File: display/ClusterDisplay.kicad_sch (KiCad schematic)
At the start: 110 parts, among them J1 Verdin iMX95 Hexa 8GB WB IT, J10 RTC coin cell, J11 Molex KK-254 22-27-2041, rota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, J2 Phoenix MKDS 1,5/3-5,08 power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, J3 Molex KK-254 22-27-2031 priva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, J4 TST040HDBC-42 panel, J8 Samtec TSW-108-07-G-S JTAG (b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, J9 Samtec TSW-104-07-G-S buttons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, Q1 PMV55ENEA (AEC-Q101, 60V/20V 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, Q2 PMV55ENEA (AEC-Q101, 60V/20V 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, Q3 PMV55ENEA ignition wake pulld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, U1 LM74930-Q1, U2 LM61460-Q1, U3 TLV767-Q1, U4 TCAN1044V-Q1, U6 TPS65131-Q1, U7 TPS61165-Q1

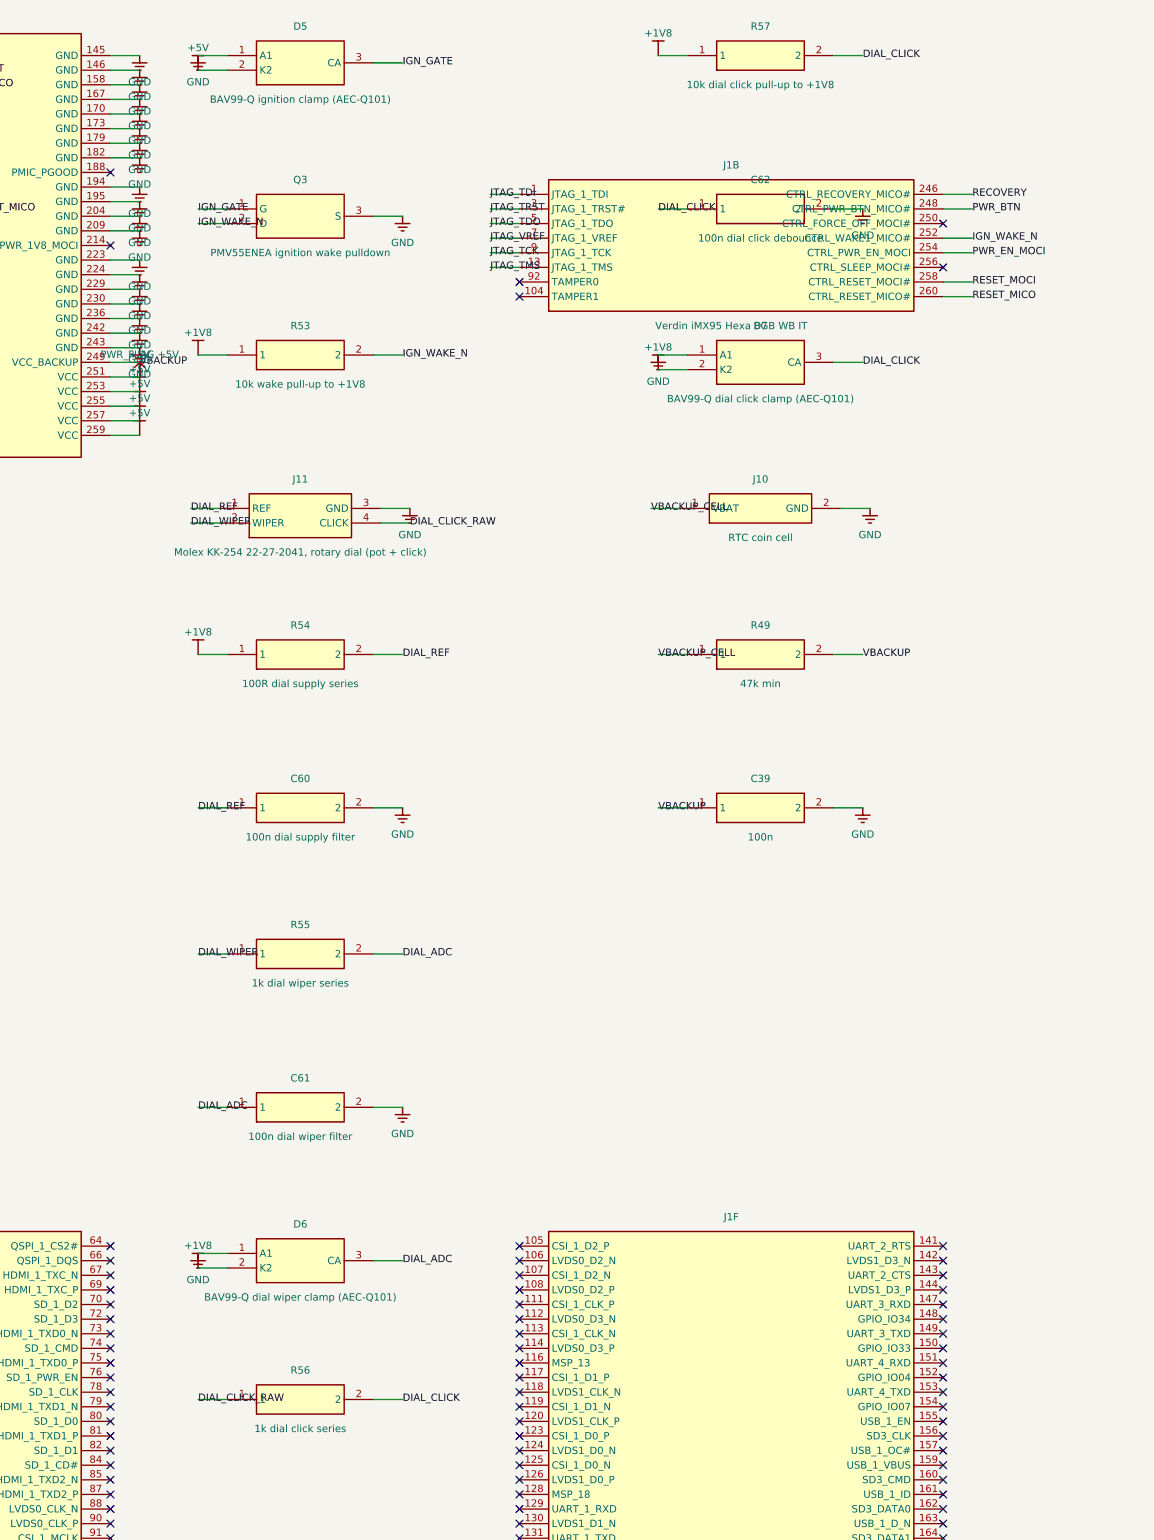
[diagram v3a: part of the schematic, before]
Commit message: display: dial interface for a Piher PSC-360 (switched 5V, scaled analog signal) plus separate click input
PSC-360 is a contactless Hall angle sensor with endless rotation; its switch output is an angle
threshold, not a push button, so J11 keeps a separate click input. Sensor 5V comes through a
TPS22918-Q1 load switch controlled by the Verdin's CTRL_SLEEP_MOCI# so it is off in suspend; the
0-5.5V ratiometric output is divided to fit the 2.1V ADC limit. ERC 0 violations, routed clean,
BOM lists the stocked PSC360G2-F1A-C0000-ERA360-05K for prototyping.

Co-Authored-By: Claude Sonnet 5.5 <noreply@anthropic.com>
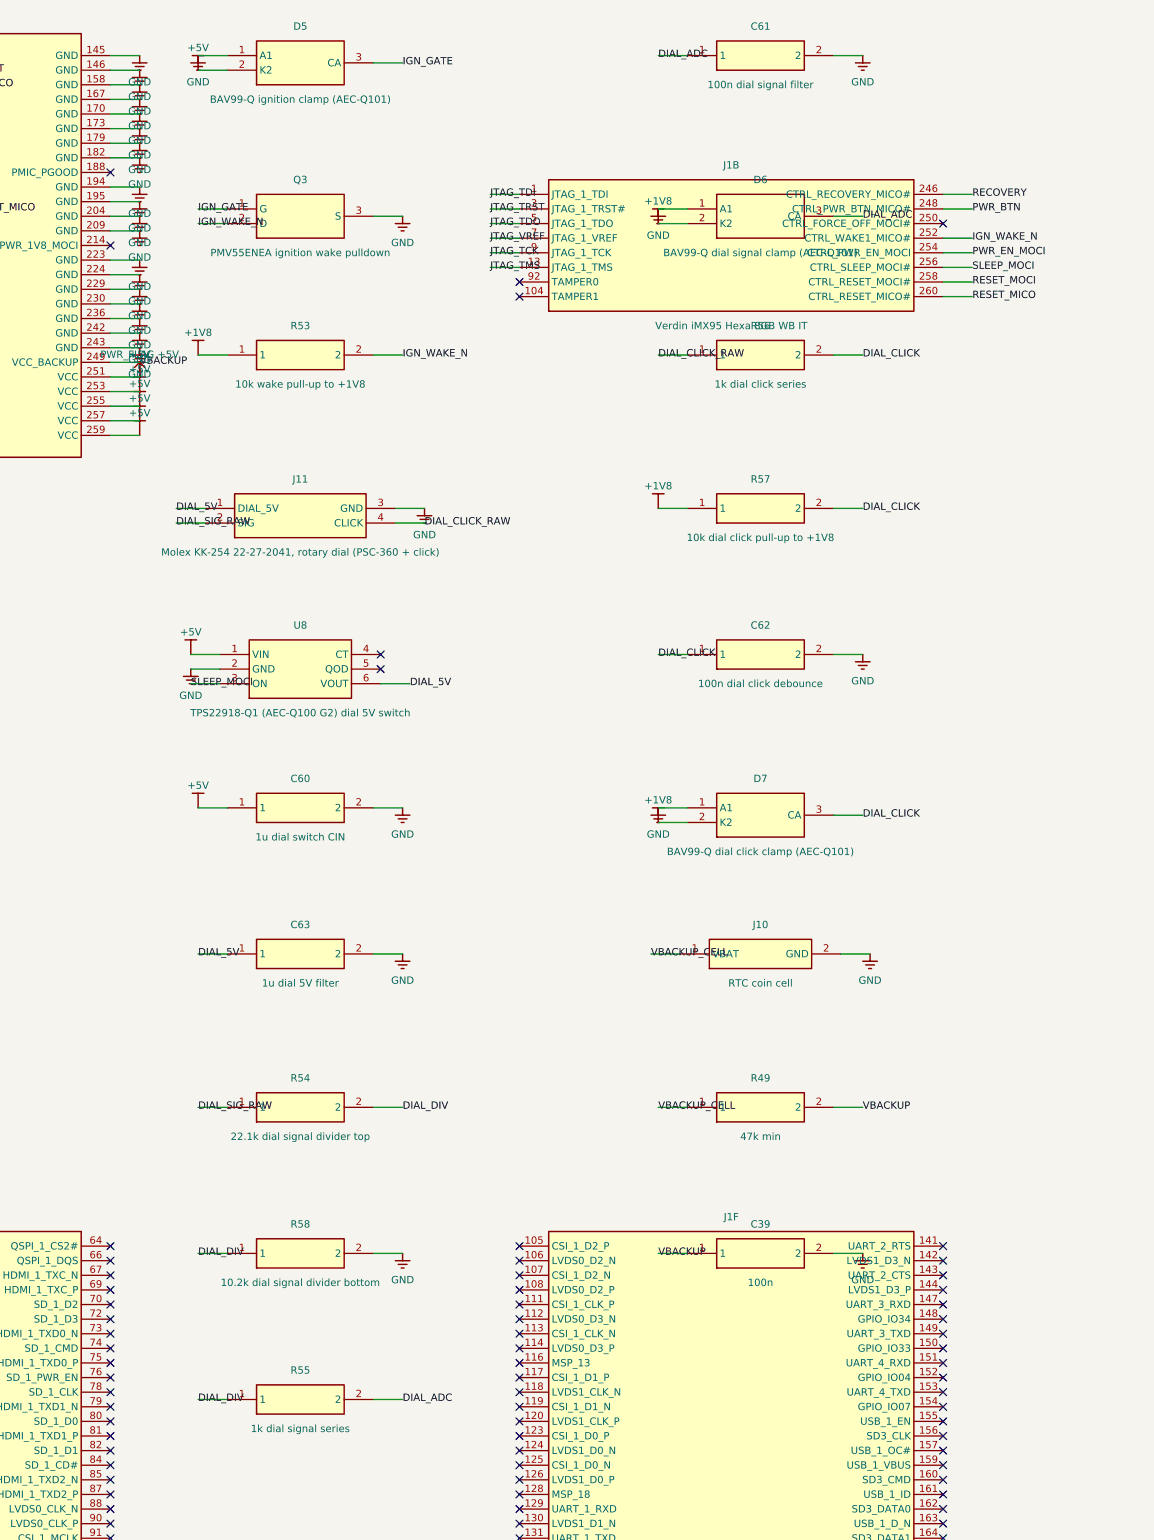
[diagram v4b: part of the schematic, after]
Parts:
- added C63: 1u dial 5V filter, Capacitor_SMD:C_0603_1608Metric, symbol ClusterDisplay:C
- added R58: 10.2k dial signal divider bottom, Resistor_SMD:R_0603_1608Metric, symbol ClusterDisplay:R
- added U8: TPS22918-Q1 (AEC-Q100 G2) dial 5V switch, Package_TO_SOT_SMD:SOT-23-6, symbol ClusterDisplay:TPS22918-Q1
- C60: value 100n dial supply filter -> 1u dial switch CIN
- C61: value 100n dial wiper filter -> 100n dial signal filter
- D6: value BAV99-Q dial wiper clamp (AEC-Q101) -> BAV99-Q dial signal clamp (AEC-Q101)
- J11: value Molex KK-254 22-27-2041, rotary dial (pot + click) -> Molex KK-254 22-27-2041, rotary dial (PSC-360 + click)
- R54: value 100R dial supply series -> 22.1k dial signal divider top
- R55: value 1k dial wiper series -> 1k dial signal series
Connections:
- net +1V8: no longer R54.1
- net +5V: now also C60.1, U8.1 (VIN)
- net GND: now also C63.2, R58.2, U8.2 (GND)
- net SLEEP_MOCI: now reaches J1.256 (CTRL_SLEEP_MOCI#)
- net SLEEP_MOCI: now also U8.3 (ON)
- removed net DIAL_REF: C60.1, J11.1 (REF), R54.2
- net DIAL_WIPER renamed DIAL_DIV
- net DIAL_DIV: now also R54.2, R58.1; no longer J11.2 (WIPER)
- new net DIAL_5V: C63.1, J11.1 (DIAL_5V), U8.6 (VOUT)
- new net DIAL_SIG_RAW: J11.2 (SIG), R54.1
- no-connect marks 197 -> 198

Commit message: Fix review findings: MOSFET pinout, gauges surge front end, converter cells, DSI
Review of 2026-10-03 found real defects; fixes and measured results:
- Nexperia PMV55ENEA/PMV37ENEA pinout is G=1, S=2, D=3: display Q1-Q3 and
  gauges Q2 had source/drain swapped. Fixed in both schematics.
- gauges/ now has the same LM74930-Q1 surge-protected front end as display/
  (5 mohm sense, OV clamp), a 5 A/32 V blade fuse on display/ (the MF-RG500 PTC
  was a 16 V part), and sender inputs with series resistor, clamp and filter.
- Converters are placed as cells around their ICs (tools/cellplace.py).
  display: SW_5V 55.6 -> 11.6 mm, boost/inverter/backlight SW 75 -> 7-13 mm,
  LM61460 input caps 57 -> 4.7-7.5 mm. gauges: SW 26.8 -> 8.7 mm, input caps 4.5 mm.
- display DSI pairs are planned by dsi_route.py after the autorouter: legs
  10.6-11.2 mm, at most 0.6 mm skew in a pair (was 64-85 mm, 21 mm skew).
- In1 is a GND plane for the router on display/ (about 925 mm of slow signals
  still cross it, down from 2615); forbidding signals there left 6-122
  connections unrouted. gauges/ keeps the old flow (planes claimed there made
  the real GND zone split into islands).
- display: USB (J13) and console UART (J12) bring-up headers, SoM and socket
  split into separate BOM lines, README rewritten.
- gauges: orderable MCU part number, DNP parts get their own BOM line and are
  left out of the placement file, 5 mohm sense resistor in the catalog.

Both boards: 0 unconnected, independent kicad-cli DRC with only accepted
categories; fab packages rebuilt. Nothing is fabricated or tested.

Co-Authored-By: Claude Sonnet 5.5 <noreply@anthropic.com>
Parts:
- added J12: Samtec TSW-103-07-G-S A55 console UART_3 1.8V (be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, Connector_PinHeader_2.54mm:PinHeader_1x03_P2.54mm_Vertical, symbol ClusterDisplay:CONN_UART
- added J13: Samtec TSW-105-07-G-S USB_1 OTG (bench only), Connector_PinHeader_2.54mm:PinHeader_1x05_P2.54mm_Vertical, symbol ClusterDisplay:CONN_USB
- F1: value MF-RG500 (Bourns, 5.0A hold/8.5A trip, AEC-Q200) -> Keystone 3568 holder, 5A Littelfuse 0297005.WXNV MINI blade fuse (32V, 1kA); footprint Fuse:Fuse_Bourns_MF-RG500 -> Fuse:Fuseholder_Blade_Mini_Keystone_3568
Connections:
- net +12V_PROT: now also Q1.3 (D); no longer Q1.2 (D)
- net COMMON: now also Q1.2 (S), Q2.2 (S); no longer Q1.3 (S), Q2.3 (S)
- net GND: now also Q3.2 (S), J12.3 (GND), J13.5 (GND); no longer Q3.3 (S)
- net IGN_WAKE_N: now also Q3.3 (D); no longer Q3.2 (D)
- net SENSE_OUT: now also Q2.3 (D); no longer Q2.2 (D)
- net UART_RXD: now reaches J1.147 (UART_3_RXD)
- net UART_RXD: now also J12.2 (RXD)
- net UART_TXD: now reaches J1.149 (UART_3_TXD)
- net UART_TXD: now also J12.1 (TXD)
- net USB_VBUS: now reaches J1.159 (USB_1_VBUS)
- net USB_VBUS: now also J13.1 (VBUS)
- net USB_ID: now reaches J1.161 (USB_1_ID)
- net USB_ID: now also J13.4 (ID)
- net USB_DN: now reaches J1.163 (USB_1_D_N)
- net USB_DN: now also J13.2 (D_N)
- net USB_DP: now reaches J1.165 (USB_1_D_P)
- net USB_DP: now also J13.3 (D_P)
- no-connect marks 198 -> 192

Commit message: display: audio path, USB-C host port and wireless-radio notes for wireless Android Auto / CarPlay
Owner decision 2026-10-16: wireless Android Auto and CarPlay with sound.

- Audio: TI TAC5112-Q1 codec (real datasheet SLASFC2A, 1.8 V I/O so no level
  shifters, no MCLK) on Verdin I2S_1 + I2C_1, 3.3 V AVDD LDO, balanced stereo
  line-out J14, electret mic J15, TPD4E05U06-Q1 ESD, reserved DNP/TBD MFi
  coprocessor access header J16 (no Apple part invented).
- USB: USB-C 2.0 host J17 on Verdin USB_2, TPS2557-Q1 VBUS switch (1.6-2.0 A),
  22k Rp (1.5 A), ESD, VBUS TVS, EN pull-down. J13 stays the bench header.
- verdin_x1: I2S_1, I2C_1 and USB_2 moved out of the unused bank; verify() updated.
- Floorplan: audio column in the left strip, connector/ESD cell leads the top
  row, USB-C cell on the bottom edge. 151.9 -> 169.3 mm wide, same height.
- Routing: 0 unconnected nets (real kicad-cli DRC); B.Cu GND pour added to stop
  In1 islands from isolating GND vias; in-place retries cut, pipeline retries up.
- cellplace: optional keepin and anchor_gap per cell.
- BOM, fab package, README, fab README, PLAN decision 6 and docs/audio-and-usb.md
  (wiring, unbalanced AUX use, antenna rules, software bring-up, unverified list).

Co-Authored-By: Claude Sonnet 5.5 <noreply@anthropic.com>
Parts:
- added C64: 10u CIN, Capacitor_SMD:C_0805_2012Metric, symbol ClusterDisplay:C_0805
- added C65: 10u COUT, Capacitor_SMD:C_0805_2012Metric, symbol ClusterDisplay:C_0805
- added C66: 10u AVDD, Capacitor_SMD:C_0805_2012Metric, symbol ClusterDisplay:C_0805
- added C67: 100n AVDD, Capacitor_SMD:C_0603_1608Metric, symbol ClusterDisplay:C
- added C68: 10u DREG, Capacitor_SMD:C_0805_2012Metric, symbol ClusterDisplay:C_0805
- added C69: 100n DREG, Capacitor_SMD:C_0603_1608Metric, symbol ClusterDisplay:C
- added C70: 10u IOVDD, Capacitor_SMD:C_0805_2012Metric, symbol ClusterDisplay:C_0805
- added C71: 100n IOVDD, Capacitor_SMD:C_0603_1608Metric, symbol ClusterDisplay:C
- added C72: 1u VREF, Capacitor_SMD:C_0603_1608Metric, symbol ClusterDisplay:C
- added C73: 1u MICBIAS, Capacitor_SMD:C_0603_1608Metric, symbol ClusterDisplay:C
- added C74, C75: 1u mic AC couple, Capacitor_SMD:C_0603_1608Metric, symbol ClusterDisplay:C
- added C76, C77, C78, C79: 4.7u line-out DC block, Capacitor_SMD:C_0805_2012Metric, symbol ClusterDisplay:C_0805
- added C80: 100n USB switch IN, Capacitor_SMD:C_0603_1608Metric, symbol ClusterDisplay:C
- added C81: 10u USB switch IN, Capacitor_SMD:C_0805_2012Metric, symbol ClusterDisplay:C_0805
- added C82: 100u 35V hybrid polymer VBUS (Panasonic EEH-ZA1V1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, Capacitor_SMD:CP_Elec_8x10, symbol ClusterDisplay:CP_HYBRID
- added D8: SMAJ5.0A VBUS TVS, Diode_SMD:D_SMA, symbol ClusterDisplay:TVS_SMA
- added J14: JST XH B5B-XH-A balanced line-out L/R, Connector_JST:JST_XH_B5B-XH-A_1x05_P2.50mm_Vertical, symbol ClusterDisplay:CONN_LINEOUT
- added J15: JST XH B3B-XH-A electret microphone (2-wire + shi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, Connector_JST:JST_XH_B3B-XH-A_1x03_P2.50mm_Vertical, symbol ClusterDisplay:CONN_MIC
- added J16: MFi coprocessor access I2C_1 + reset (TBD, DNP), Connector_PinHeader_2.54mm:PinHeader_1x04_P2.54mm_Vertical, symbol ClusterDisplay:CONN_MFI
- added J17: GCT USB4105-GF-A USB-C 2.0 host receptacle, Connector_USB:USB_C_Receptacle_GCT_USB4105-xx-A_16P_TopMnt_Horizontal, symbol ClusterDisplay:CONN_USBC
- added R59: 316k 1% FB top, Resistor_SMD:R_0603_1608Metric, symbol ClusterDisplay:R
- added R60: 100k FB bot, Resistor_SMD:R_0603_1608Metric, symbol ClusterDisplay:R
- added R61: 2.2k I2C1 SDA pull-up, Resistor_SMD:R_0603_1608Metric, symbol ClusterDisplay:R
- added R62: 2.2k I2C1 SCL pull-up, Resistor_SMD:R_0603_1608Metric, symbol ClusterDisplay:R
- added R63: 2.2k mic bias, Resistor_SMD:R_0603_1608Metric, symbol ClusterDisplay:R
- added R64: 100R mic return, Resistor_SMD:R_0603_1608Metric, symbol ClusterDisplay:R
- added R65, R66, R67, R68: 100R line-out series, Resistor_SMD:R_0603_1608Metric, symbol ClusterDisplay:R
- added R69: 61.9k 1% USB ILIM (1.6-2.0 A), Resistor_SMD:R_0603_1608Metric, symbol ClusterDisplay:R
- added R70: 100k FAULT pull-up to +1V8, Resistor_SMD:R_0603_1608Metric, symbol ClusterDisplay:R
- added R71: 22k Rp CC1 (1.5 A, +/-5 percent or better), Resistor_SMD:R_0603_1608Metric, symbol ClusterDisplay:R
- added R72: 22k Rp CC2 (1.5 A, +/-5 percent or better), Resistor_SMD:R_0603_1608Metric, symbol ClusterDisplay:R
- added R73: 100k USB EN pull-down, Resistor_SMD:R_0603_1608Metric, symbol ClusterDisplay:R
- added U10: TLV767-Q1 (3.3 V audio AVDD), Package_DFN_QFN:Texas_DRB0008A, symbol ClusterDisplay:TLV767-Q1
- added U11: TPS2557-Q1, Package_DFN_QFN:Texas_DRB0008A, symbol ClusterDisplay:TPS2557-Q1
- added U12: TPD4E05U06-Q1 line-out ESD, Package_SON:USON-10_2.5x1.0mm_P0.5mm, symbol ClusterDisplay:TPD4E05U06-Q1
- added U13: TPD4E05U06-Q1 mic ESD, Package_SON:USON-10_2.5x1.0mm_P0.5mm, symbol ClusterDisplay:TPD4E05U06-Q1
- added U14: TPD4E05U06-Q1 USB ESD, Package_SON:USON-10_2.5x1.0mm_P0.5mm, symbol ClusterDisplay:TPD4E05U06-Q1
- added U9: TAC5112-Q1, Package_DFN_QFN:QFN-32-1EP_5x5mm_P0.5mm_EP3.7x3.7mm_ThermalVias, symbol ClusterDisplay:TAC5112-Q1
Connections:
- net +1V8: now also C70.1, C71.1, R61.2, R62.2, R70.2, U9.7 (IOVDD)
- net +5V: now also C64.1, C80.1, C81.1, R71.2, R72.2, U10.8 (IN), U11.2 (IN1), U11.3 (IN2)
- net GND: now also C64.2, C65.2, C66.2, C67.2, C68.2, C69.2, C70.2, C71.2, C72.2, C73.2, C80.2, C81.2, C82.2, D8.2, J14.5 (GND), J15.3 (GND), J16.4 (GND), J17.A1 (A1_GND), J17.A12 (A12_GND), J17.B1 (B1_GND), J17.B12 (B12_GND), J17.SH (SHIELD), R60.2, R64.2, R69.2, R73.2, U10.4 (GND), U10.6 (GND2), U10.9 (EP), U11.1 (GND), U11.9 (EP), U12.3 (GND1), U12.8 (GND2), U13.3 (GND1), U13.8 (GND2), U14.3 (GND1), U14.8 (GND2), U9.1 (VSS1), U9.15 (VSS3), U9.16 (ADDR), U9.22 (VSSI1), U9.23 (VSSI2), U9.24 (VSSI3), U9.25 (VSSI4), U9.26 (VSS4), U9.33 (EP), U9.8 (VSS2)
- net PWR_EN_MOCI: now also U10.5 (EN)
- net MFI_RST_N: now reaches J1.208 (GPIO_2)
- net MFI_RST_N: now also J16.3 (RST_N)
- new net +3V3: C65.1, C66.1, C67.1, R59.1, U10.1 (OUT), U9.31 (AVDD)
- new net AOUT_L_N: R66.1, U9.27 (OUT1M)
- new net AOUT_L_N_R: C77.1, R66.2
- new net AOUT_L_P: R65.1, U9.28 (OUT1P)
- new net AOUT_L_P_R: C76.1, R65.2
- new net AOUT_R_N: R68.1, U9.30 (OUT2M)
- new net AOUT_R_N_R: C79.1, R68.2
- new net AOUT_R_P: R67.1, U9.29 (OUT2P)
- new net AOUT_R_P_R: C78.1, R67.2
- new net CODEC_DREG: C68.1, C69.1, U9.2 (DREG)
- new net CODEC_MICBIAS: C73.1, R63.1, U9.17 (MICBIAS)
- new net CODEC_VREF: C72.1, U9.32 (VREF)
- new net FB_3V3: R59.2, R60.1, U10.3 (FB)
- new net I2C1_SCL: J1.14 (I2C_1_SCL), J16.2 (SCL), R62.1, U9.9 (SCL)
- new net I2C1_SDA: J1.12 (I2C_1_SDA), J16.1 (SDA), R61.1, U9.10 (SDA)
- new net I2S_BCLK: J1.30 (I2S_1_BCLK), U9.3 (BCLK)
- new net I2S_DIN: J1.34 (I2S_1_D_OUT), U9.6 (DIN)
- new net I2S_DOUT: J1.36 (I2S_1_D_IN), U9.5 (DOUT)
- new net I2S_FSYNC: J1.32 (I2S_1_SYNC), U9.4 (FSYNC)
- new net LINE_L_N: C77.2, J14.2 (L_N), U12.2 (CH2)
- new net LINE_L_P: C76.2, J14.1 (L_P), U12.1 (CH1)
- new net LINE_R_N: C79.2, J14.4 (R_N), U12.5 (CH4)
- new net LINE_R_P: C78.2, J14.3 (R_P), U12.4 (CH3)
- new net MIC_IN_N: C75.2, U9.19 (IN1M)
- new net MIC_IN_P: C74.2, U9.18 (IN1P)
- new net MIC_N: C75.1, J15.2 (MIC_N), R64.1, U13.2 (CH2)
- new net MIC_P: C74.1, J15.1 (MIC_P), R63.2, U13.1 (CH1)
- new net USB2_CC1: J17.A5 (A5_CC1), R71.1, U14.4 (CH3)
- new net USB2_CC2: J17.B5 (B5_CC2), R72.1, U14.5 (CH4)
- new net USB2_DN: J1.181 (USB_2_D_N), J17.A7 (A7_DN), J17.B7 (B7_DN), U14.2 (CH2)
- new net USB2_DP: J1.183 (USB_2_D_P), J17.A6 (A6_DP), J17.B6 (B6_DP), U14.1 (CH1)
- new net USB2_EN: J1.185 (USB_2_EN), R73.1, U11.4 (EN)
- new net USB2_ILIM: R69.1, U11.5 (ILIM)
- new net USB2_OC_N: J1.187 (USB_2_OC#), R70.1, U11.8 (FAULT)
- new net USB2_VBUS: C82.1, D8.1, J17.A9 (A9_VBUS), J17.B4 (B4_VBUS), U11.6 (OUT1), U11.7 (OUT2)
- new net USB2_VBUS_L: J17.A4 (A4_VBUS), J17.B9 (B9_VBUS)
- no-connect marks 192 -> 205

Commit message: Electrical review, part 2: +3V3 rail clamp on gauges, display battery path and TVS footprint, harness wording, new display parts reviewed
gauges/: D33 (onsemi SZMMSZ3V6T1G 3.6 V zener) clamps +3V3 when a sender wire is shorted to battery with the car off (G-08); BOM and connector values follow docs/harness.md (J7 DTM06-6S with a sealed cavity, J8 an in-dash KK 254 cable, 20/22 AWG). display/: D1 footprint D_SMB -> D_SMC to match the SMCJ33A in the BOM (D-01); VBAT_IN, VBAT_F, SENSE_OUT and COMMON added to TRUNK_NETS (D-02). review/expected.py covers the TAC5112-Q1, TPS2557-Q1, TPD4E05U06-Q1 and the second TLV767-Q1. Both boards regenerated and routed: real kicad-cli DRC 0 unconnected, only accepted categories; fab packages rebuilt.

Co-Authored-By: Claude Opus 5.5 <noreply@anthropic.com>
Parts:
- D1: footprint Diode_SMD:D_SMB -> Diode_SMD:D_SMC
